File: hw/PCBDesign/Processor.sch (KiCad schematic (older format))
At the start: 5 parts

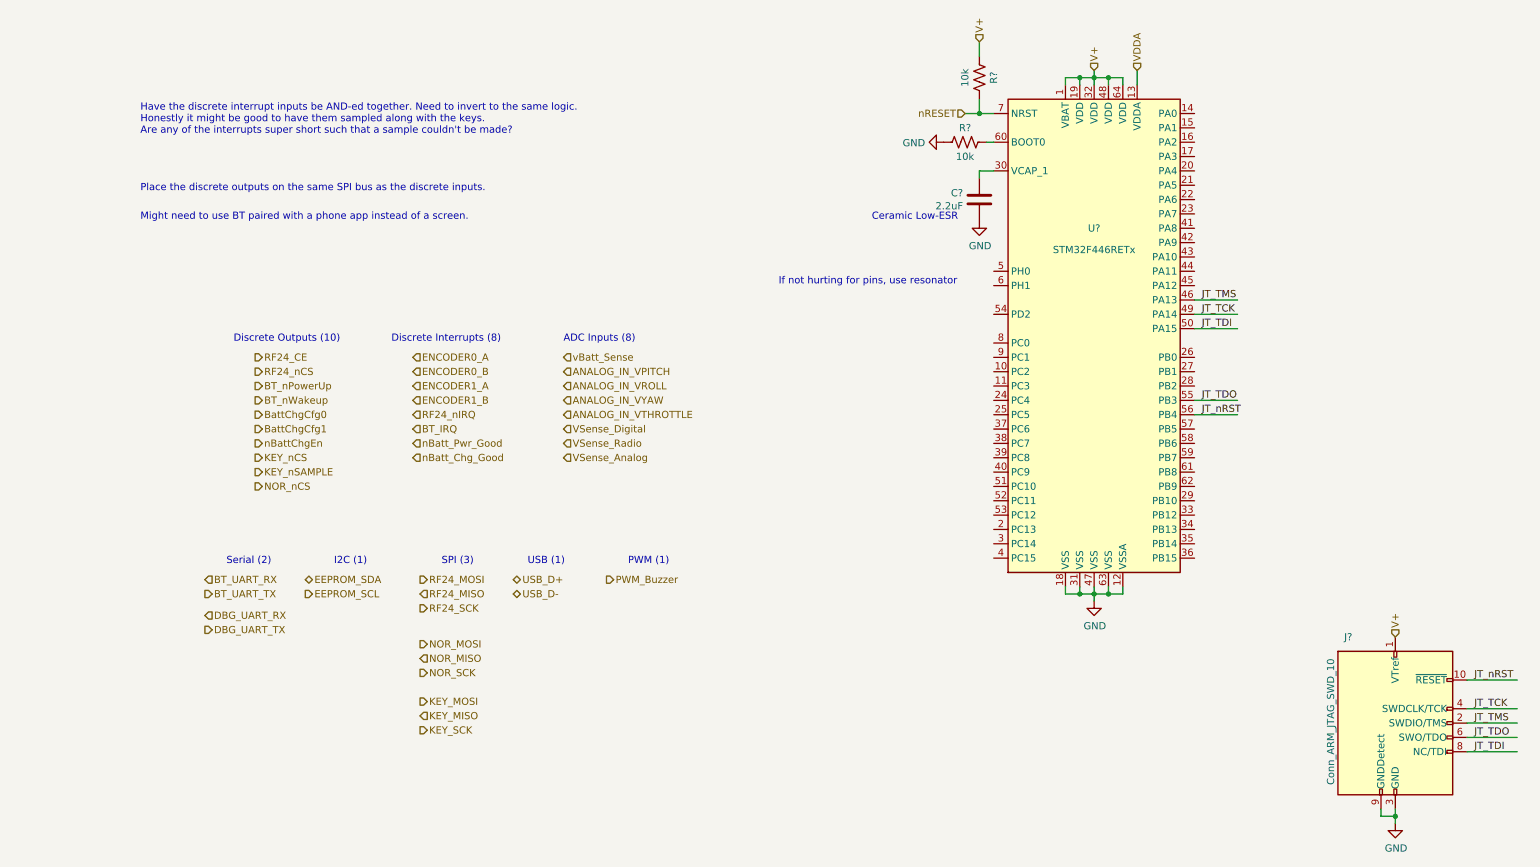
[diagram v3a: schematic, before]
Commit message: Wire some of the protocols
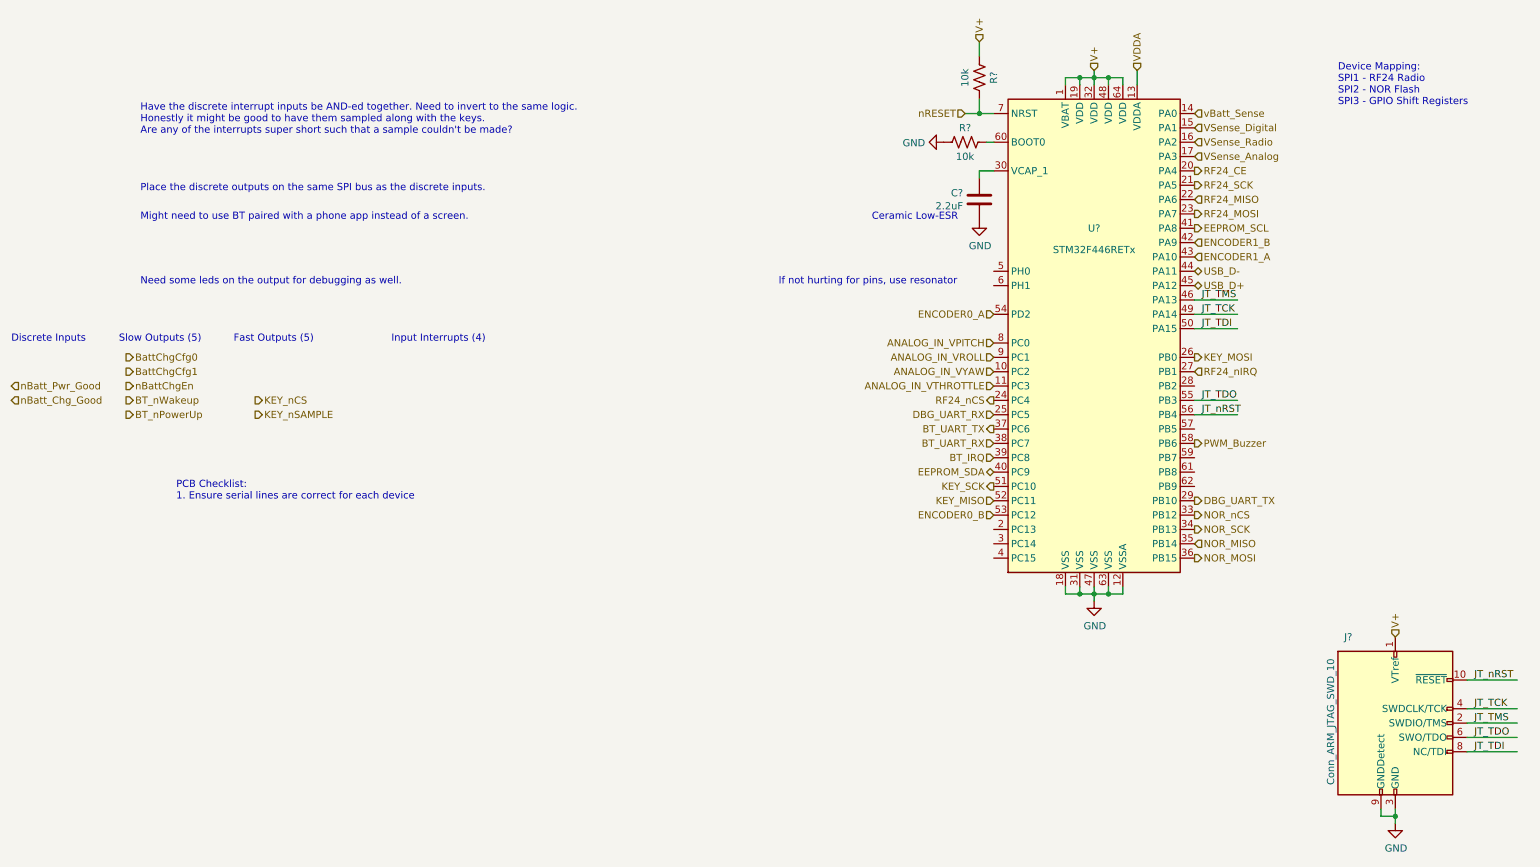
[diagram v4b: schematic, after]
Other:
- note added: "Device Mapping:\nSPI1 - RF24 Radio\nSPI2 - NOR Flash\nSPI3 - GPIO Shift Registers"
- note added: "Discrete Inputs"
- note added: "Fast Outputs (5)"
- note added: "Input Interrupts (4)"
- note added: "Need some leds on the output for debugging as well."
- note added: "PCB Checklist:\n1. Ensure serial lines are correct for each device"
- note added: "Slow Outputs (5)"
- note removed: "ADC Inputs (8)"
- note removed: "Discrete Interrupts (8)"
- note removed: "Discrete Outputs (10)"
- note removed: "I2C (1)"
- note removed: "PWM (1)"
- note removed: "SPI (3)"
- note removed: "Serial (2)"
- note removed: "USB (1)"
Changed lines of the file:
@@
 	1    0    0    -1
 $EndComp
-Text HLabel 4050 4650 2    50   BiDi ~ 0
+Text HLabel 8800 2600 2    50   BiDi ~ 0
 USB_D+
-Text HLabel 4050 4750 2    50   BiDi ~ 0
+Text HLabel 8800 2500 2    50   BiDi ~ 0
 USB_D-
-Text HLabel 3350 3700 2    50   Input ~ 0
+Text HLabel 550  3300 2    50   Input ~ 0
 nBatt_Pwr_Good
-Text HLabel 3350 3800 2    50   Input ~ 0
+Text HLabel 550  3400 2    50   Input ~ 0
 nBatt_Chg_Good
-Text HLabel 4400 3100 2    50   Input ~ 0
+Text HLabel 8800 1400 2    50   Input ~ 0
 vBatt_Sense
-Text HLabel 2250 3700 2    50   Output ~ 0
+Text HLabel 1350 3300 2    50   Output ~ 0
 nBattChgEn
-Text HLabel 2250 3500 2    50   Output ~ 0
+Text HLabel 1350 3100 2    50   Output ~ 0
 BattChgCfg0
-Text HLabel 2250 3600 2    50   Output ~ 0
+Text HLabel 1350 3200 2    50   Output ~ 0
 BattChgCfg1
-Text HLabel 1900 4650 2    50   Input ~ 0
+Text HLabel 7400 3700 0    50   Input ~ 0
 BT_UART_RX
-Text HLabel 1900 4750 2    50   Output ~ 0
+Text HLabel 7400 3600 0    50   Output ~ 0
 BT_UART_TX
-Text HLabel 2250 3400 2    50   Output ~ 0
+Text HLabel 1350 3400 2    50   Output ~ 0
 BT_nWakeup
-Text HLabel 2250 3300 2    50   Output ~ 0
+Text HLabel 1350 3500 2    50   Output ~ 0
 BT_nPowerUp
-Text HLabel 3350 3600 2    50   Input ~ 0
+Text HLabel 7400 3800 0    50   Input ~ 0
 BT_IRQ
-Text HLabel 3400 4650 2    50   Output ~ 0
+Text HLabel 8800 2100 2    50   Output ~ 0
 RF24_MOSI
-Text HLabel 3400 4750 2    50   Input ~ 0
+Text HLabel 8800 2000 2    50   Input ~ 0
 RF24_MISO
-Text HLabel 3400 4850 2    50   Output ~ 0
+Text HLabel 8800 1900 2    50   Output ~ 0
 RF24_SCK
-Text HLabel 2250 3200 2    50   Output ~ 0
+Text HLabel 7400 3400 0    50   Output ~ 0
 RF24_nCS
-Text HLabel 2250 3100 2    50   Output ~ 0
+Text HLabel 8800 1800 2    50   Output ~ 0
 RF24_CE
-Text HLabel 3350 3500 2    50   Input ~ 0
+Text HLabel 8800 3200 2    50   Input ~ 0
 RF24_nIRQ
-Text HLabel 3400 5100 2    50   Output ~ 0
+Text HLabel 8800 4500 2    50   Output ~ 0
 NOR_MOSI
-Text HLabel 3400 5200 2    50   Input ~ 0
+Text HLabel 8800 4400 2    50   Input ~ 0
 NOR_MISO
-Text HLabel 3400 5300 2    50   Output ~ 0
+Text HLabel 8800 4300 2    50   Output ~ 0
 NOR_SCK
-Text HLabel 2250 4000 2    50   Output ~ 0
+Text HLabel 8800 4200 2    50   Output ~ 0
 NOR_nCS
-Text HLabel 2600 4650 2    50   BiDi ~ 0
+Text HLabel 7400 3900 0    50   BiDi ~ 0
 EEPROM_SDA
-Text HLabel 2600 4750 2    50   Output ~ 0
+Text HLabel 8800 2200 2    50   Output ~ 0
 EEPROM_SCL
-Text HLabel 4400 3600 2    50   Input ~ 0
+Text HLabel 8800 1500 2    50   Input ~ 0
 VSense_Digital
-Text HLabel 4400 3700 2    50   Input ~ 0
+Text HLabel 8800 1600 2    50   Input ~ 0
 VSense_Radio
-Text HLabel 4400 3800 2    50   Input ~ 0
+Text HLabel 8800 1700 2    50   Input ~ 0
 VSense_Analog
 Text HLabel 8100 1100 1    50   Input ~ 0
@@
 Text HLabel 7200 1400 0    50   Input ~ 0
 nRESET
-Text HLabel 4700 4650 2    50   Output ~ 0
+Text HLabel 8800 3700 2    50   Output ~ 0
 PWM_Buzzer
-Text HLabel 3400 5500 2    50   Output ~ 0
+Text HLabel 8800 3100 2    50   Output ~ 0
 KEY_MOSI
-Text HLabel 3400 5600 2    50   Input ~ 0
+Text HLabel 7400 4100 0    50   Input ~ 0
 KEY_MISO
-Text HLabel 3400 5700 2    50   Output ~ 0
+Text HLabel 7400 4000 0    50   Output ~ 0
 KEY_SCK
-Text HLabel 2250 3800 2    50   Output ~ 0
+Text HLabel 2250 3400 2    50   Output ~ 0
 KEY_nCS
-Text HLabel 2250 3900 2    50   Output ~ 0
+Text HLabel 2250 3500 2    50   Output ~ 0
 KEY_nSAMPLE
-Text HLabel 3350 3100 2    50   Input ~ 0
+Text HLabel 7400 2800 0    50   Input ~ 0
 ENCODER0_A
-Text HLabel 3350 3200 2    50   Input ~ 0
+Text HLabel 7400 4200 0    50   Input ~ 0
 ENCODER0_B
-Text HLabel 3350 3300 2    50   Input ~ 0
+Text HLabel 8800 2400 2    50   Input ~ 0
 ENCODER1_A
-Text HLabel 3350 3400 2    50   Input ~ 0
+Text HLabel 8800 2300 2    50   Input ~ 0
 ENCODER1_B
-Text HLabel 4400 3200 2    50   Input ~ 0
+Text HLabel 7400 3000 0    50   Input ~ 0
 ANALOG_IN_VPITCH
-Text HLabel 4400 3300 2    50   Input ~ 0
+Text HLabel 7400 3100 0    50   Input ~ 0
 ANALOG_IN_VROLL
-Text HLabel 4400 3400 2    50   Input ~ 0
+Text HLabel 7400 3200 0    50   Input ~ 0
 ANALOG_IN_VYAW
-Text HLabel 4400 3500 2    50   Input ~ 0
+Text HLabel 7400 3300 0    50   Input ~ 0
 ANALOG_IN_VTHROTTLE
 Wire Wire Line
@@
 Text Notes 5900 2600 0    50   ~ 0
 If not hurting for pins, use resonator
-Text Notes 4400 3000 0    50   ~ 0
-ADC Inputs (8)
 Text Notes 3200 3000 0    50   ~ 0
-Discrete Interrupts (8)
+Input Interrupts (4)
 Text Notes 2100 3000 0    50   ~ 0
-Discrete Outputs (10)
-Text Notes 2050 4550 0    50   ~ 0
-Serial (2)
-Text Notes 2800 4550 0    50   ~ 0
-I2C (1)
-Text Notes 3550 4550 0    50   ~ 0
-SPI (3)
-Text Notes 4150 4550 0    50   ~ 0
-USB (1)
-Text Notes 4850 4550 0    50   ~ 0
-PWM (1)
-Text HLabel 1900 5000 2    50   Output ~ 0
+Fast Outputs (5)
+Text HLabel 8800 4100 2    50   Output ~ 0
 DBG_UART_TX
-Text HLabel 1900 4900 2    50   Input ~ 0
+Text HLabel 7400 3500 0    50   Input ~ 0
 DBG_UART_RX
 Text Notes 1450 1950 0    50   ~ 0
@@
 Text Notes 1450 2150 0    50   ~ 0
 Might need to use BT paired with a phone app instead of a screen.
+Text Notes 550  3000 0    50   ~ 0
+Discrete Inputs
+Text Notes 1300 3000 0    50   ~ 0
+Slow Outputs (5)
+Text Notes 1700 4100 0    50   ~ 0
+PCB Checklist:\n1. Ensure serial lines are correct for each device
+Text Notes 9800 1350 0    50   ~ 0
+Device Mapping:\nSPI1 - RF24 Radio\nSPI2 - NOR Flash\nSPI3 - GPIO Shift Registers
+Text Notes 1450 2600 0    50   ~ 0
+Need some leds on the output for debugging as well.
 $EndSCHEMATC

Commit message: Finished initial schematic design
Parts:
- added C? (x2): 100n, symbol Device:C
- added C? (x2): C, symbol Device:C
- added D? (x4): LED, symbol Device:LED
- added R? (x4): 10k, symbol Device:R_US
- added R? (x4): 560, symbol Device:R_US
- added U? (x2): 74HC595, symbol 74xx:74HC595
- added Y?: Crystal, symbol Device:Crystal
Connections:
- net labels added: KeyOut_nCS, nBatteryChargeGood, nBatteryPowerGood
- wire segments 42 -> 84
- no-connect marks 0 -> 8
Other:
- note added: "GPIO Outputs"
- note added: "PCB Checklist: \n https://github.com/azonenberg/pcb-checklist\n1. Ensure serial lines are correct for each device\n2. Verify the shift register connections match the pin names\n3. Verify interrupt lines are all separated and can fire individually."
- note added: "Pipe this out to the shift registers for the moment..."
- note removed: "Discrete Inputs"
- note removed: "Fast Outputs (5)"
- note removed: "Have the discrete interrupt inputs be AND-ed together. Need to invert to the same logic.\nHonestly it might be good to have them sampled along with the keys.\nAre any of the interrupts super short such that a sample couldn't be made?"
- note removed: "If not hurting for pins, use resonator"
- note removed: "Input Interrupts (4)"
- note removed: "Might need to use BT paired with a phone app instead of a screen."
- note removed: "Need some leds on the output for debugging as well."
- note removed: "PCB Checklist:\n1. Ensure serial lines are correct for each device"
- note removed: "Place the discrete outputs on the same SPI bus as the discrete inputs."
- note removed: "Slow Outputs (5)"

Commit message: Clean up schematics some
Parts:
- Y?: value Crystal -> 8MHz Crystal
- gave numbers to parts that had none: 1
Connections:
- net labels added: BT_VCC_EN, RF24_VCC_EN
- no-connect marks 8 -> 6
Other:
- note added: "Debug LEDs"
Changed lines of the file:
@@
 NoConn ~ 3350 3850
 NoConn ~ 3350 3750
-NoConn ~ 3350 2500
-NoConn ~ 3350 2400
 $Comp
 L Device:Crystal Y?
@@
 P 6400 2500
 F 0 "Y?" V 6354 2631 50  0000 L CNN
-F 1 "Crystal" V 6445 2631 50  0000 L CNN
+F 1 "8MHz Crystal" V 6445 2631 50  0000 L CNN
 F 2 "" H 6400 2500 50  0001 C CNN
 F 3 "~" H 6400 2500 50  0001 C CNN
@@
 $EndComp
 $Comp
-L Device:C C?
+L Device:C 1.5pF
 U 1 1 604DDB41
 P 6150 2300
-F 0 "C?" V 6050 2400 50  0000 C CNN
+F 0 "1.5pF" V 6300 2300 50  0000 C CNN
 F 1 "C" V 5989 2300 50  0000 C CNN
 F 2 "" H 6188 2150 50  0001 C CNN
@@
 $EndComp
 $Comp
-L Device:C C?
+L Device:C 1.5pF
 U 1 1 604DE10D
 P 6150 2700
-F 0 "C?" V 6050 2800 50  0000 C CNN
+F 0 "1.5pF" V 6300 2700 50  0000 C CNN
 F 1 "C" V 5989 2700 50  0000 C CNN
 F 2 "" H 6188 2550 50  0001 C CNN
@@
 	6850 2700 6850 2600
 Connection ~ 6400 2700
+Text HLabel 3350 2400 2    50   Output ~ 0
+BT_VCC_EN
+Text HLabel 3350 2500 2    50   Output ~ 0
+RF24_VCC_EN
+Text Notes 3800 5600 0    50   ~ 0
+Debug LEDs
 $EndSCHEMATC

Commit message: Schematic polishing
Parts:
- C50, C51: renamed from C?; footprint (none) -> Capacitor_SMD:C_0402_1005Metric; LCSC (none) -> C1525
- C52: renamed from C?; footprint (none) -> Capacitor_SMD:C_0805_2012Metric; LCSC (none) -> C49217
- C53, C54: renamed from 1.5pF; value C -> 1.5pF; footprint (none) -> Capacitor_SMD:C_0402_1005Metric; LCSC (none) -> C1552
- D3: renamed from D?; value LED -> DBG_LED_3; footprint (none) -> LED_SMD:LED_0603_1608Metric; LCSC (none) -> C72041
- D4: renamed from D?; value LED -> DBG_LED_2; footprint (none) -> LED_SMD:LED_0603_1608Metric; LCSC (none) -> C72041
- D5: renamed from D?; value LED -> DBG_LED_1; footprint (none) -> LED_SMD:LED_0603_1608Metric; LCSC (none) -> C72041
- D6: renamed from D?; value LED -> DBG_LED_0; footprint (none) -> LED_SMD:LED_0603_1608Metric; LCSC (none) -> C72041
- J4: renamed from J?; footprint (none) -> Connector_PinHeader_1.27mm:PinHeader_2x05_P1.27mm_Vertical_SMD
- R88, R89, R90, R91, R96, R97: renamed from R?; footprint (none) -> Resistor_SMD:R_0402_1005Metric; LCSC (none) -> C25744
- R92, R93, R94, R95: renamed from R?; footprint (none) -> Resistor_SMD:R_0402_1005Metric; LCSC (none) -> C11702
- U11, U12: renamed from U?; footprint (none) -> Package_SO:SO-16_3.9x9.9mm_P1.27mm; LCSC (none) -> C5947
- Y1: renamed from Y?; footprint (none) -> Crystal:Crystal_SMD_5032-2Pin_5.0x3.2mm
- gave numbers to parts that had none: 1

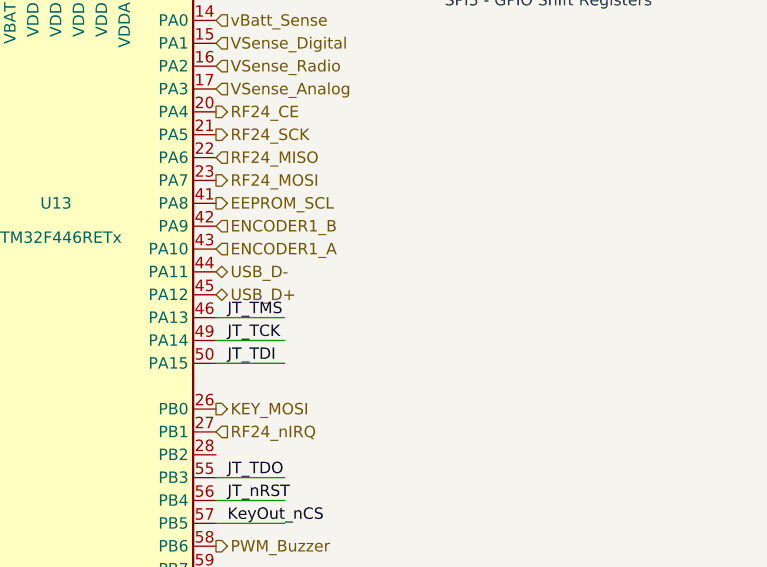
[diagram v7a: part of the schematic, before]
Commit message: Laid out power section
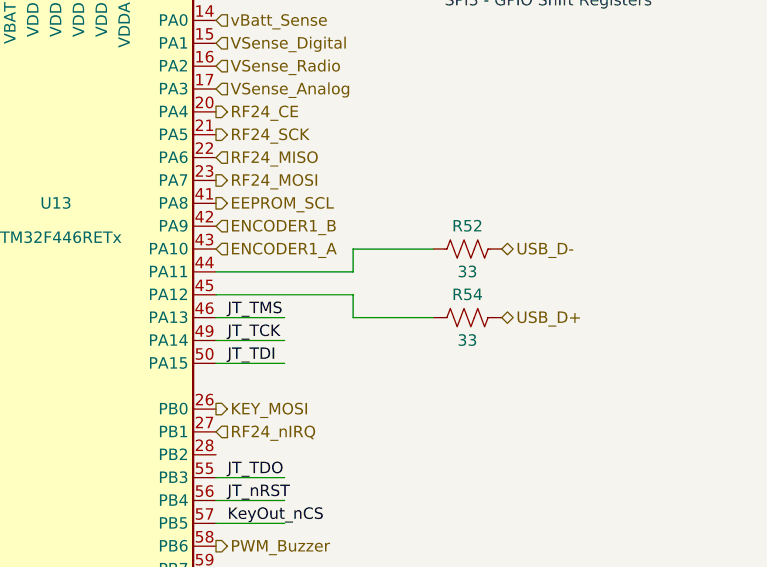
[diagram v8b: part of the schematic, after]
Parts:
- added R52, R54: 33, Resistor_SMD:R_0402_1005Metric, symbol Device:R_US
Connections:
- wire segments 84 -> 90
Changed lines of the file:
@@
 	1    0    0    -1
 $EndComp
-Text HLabel 8800 2600 2    50   BiDi ~ 0
+Text HLabel 10050 2700 2    50   BiDi ~ 0
 USB_D+
-Text HLabel 8800 2500 2    50   BiDi ~ 0
+Text HLabel 10050 2400 2    50   BiDi ~ 0
 USB_D-
 Text HLabel 8100 5600 2    50   Input ~ 0
@@
 Text Notes 3800 5600 0    50   ~ 0
 Debug LEDs
+$Comp
+L Device:R_US R52
+U 1 1 605FAE0B
+P 9900 2400
+F 0 "R52" V 9800 2400 50  0000 C CNN
+F 1 "33" V 10000 2400 50  0000 C CNN
+F 2 "Resistor_SMD:R_0402_1005Metric" V 9940 2390 50  0001 C CNN
+F 3 "~" H 9900 2400 50  0001 C CNN
+F 4 "C25105" H 9900 2400 50  0001 C CNN "LCSC"
+	1    9900 2400
+	0    1    1    0
+$EndComp
+$Comp
+L Device:R_US R54
+U 1 1 605FB594
+P 9900 2700
+F 0 "R54" V 9800 2700 50  0000 C CNN
+F 1 "33" V 10000 2700 50  0000 C CNN
+F 2 "Resistor_SMD:R_0402_1005Metric" V 9940 2690 50  0001 C CNN
+F 3 "~" H 9900 2700 50  0001 C CNN
+F 4 "C25105" H 9900 2700 50  0001 C CNN "LCSC"
+	1    9900 2700
+	0    1    1    0
+$EndComp
+Wire Wire Line
+	9750 2700 9400 2700
+Wire Wire Line
+	9400 2700 9400 2600
+Wire Wire Line
+	9400 2600 8800 2600
+Wire Wire Line
+	9750 2400 9400 2400
+Wire Wire Line
+	9400 2400 9400 2500
+Wire Wire Line
+	9400 2500 8800 2500
 $EndSCHEMATC
